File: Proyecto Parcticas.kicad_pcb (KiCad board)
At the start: 2 copper layers, 53.4 x 79.4 mm, 18 parts, among them J2 Molex_KK-254_AE-6410-06A_1x06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, U1 Sensor_de_corriente_ACS758LCB

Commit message: Ultima version
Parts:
- added C4: 100nF, Capacitor_SMD:C_1206_3216Metric, F.Cu at (157.7, 110.2)
- added D1: 1N4752, Diode_SMD:D_MiniMELF, F.Cu at (161.8, 129.0)
- added J3: Baterias, Connector_Molex:Molex_KK-254_AE-6410-02A_1x02_P2.54mm_Vertical, B.Cu at (182.8, 136.4)
- added R1: 100k, Resistor_SMD:R_1206_3216Metric, F.Cu at (157.7, 135.4)
- added R2: 100k, Resistor_SMD:R_1206_3216Metric, F.Cu at (157.7, 132.8)
- added R3: 1M, Resistor_SMD:R_1206_3216Metric, F.Cu at (157.7, 130.3)
- added R4: 100k, Resistor_SMD:R_1206_3216Metric, F.Cu at (157.7, 127.5)
- C2, C3: moved to B.Cu
- moved C3 41.0 mm to (182.5, 100.0), turned to 90 degrees
- moved C2 28.0 mm to (140.5, 78.6), turned to 90 degrees
- moved S1 1.70 mm to (182.9, 125.5)
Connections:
- C2 pad 1: VCC -> unconnected-(C2-Pad1)
- C3 pad 1: EN -> Net-(C3-Pad1)
- E1 pad 1: E_CLK -> (no net)
- E1 pad 2: E_DT -> (no net)
- E1 pad 3: E_SW -> (no net)
- E1 pad 4: VCC -> (no net)
- E1 pad 5: GND -> (no net)
- S2 pad : B+ -> (no net)
- S2 pad 1: A+ -> Net-(S2-Pad1)
- S2 pad 2: A- -> Net-(S2-Pad2)
- S2 pad 3: E+ -> Net-(S2-Pad3)
- S2 pad 4: E- -> Net-(S2-Pad4)
- S3 pad 1: E+ -> (no net)
- S3 pad 2: E- -> (no net)
- S3 pad 3: A- -> (no net)
- S3 pad 4: A+ -> (no net)
- U1 pad 1: GND -> (no net)
- U1 pad 2: VCC -> (no net)
- U1 pad 3: S_C_OU1 -> (no net)
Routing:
- net GND: track 234.2 -> 316.7 mm, vias 0 -> 2
- net Net-(C3-Pad1): track 0.00 -> 69.9 mm
- net BAText+: track 0.00 -> 33.3 mm
- net BATint+: track 0.00 -> 27.9 mm
- net EN: track 9.46 -> 34.7 mm
- net Net-(S2-Pad3): track 0.00 -> 10.7 mm
- net E+: track 10.7 -> 0.00 mm
- net Net-(S2-Pad4): track 0.00 -> 10.7 mm
- net E-: track 10.7 -> 0.00 mm
- net Net-(S2-Pad2): track 0.00 -> 10.7 mm
- net A-: track 10.7 -> 0.00 mm
- net Net-(S2-Pad1): track 0.00 -> 10.7 mm
- net A+: track 10.7 -> 0.00 mm
- net BAT+_EXT: track 0.00 -> 8.80 mm
- net BAT+_INT: track 0.00 -> 8.55 mm
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
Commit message: Ultima super mejorada
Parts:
- removed the REF** at (145.0, 115.3)
- removed the REF** at (177.7, 119.3)
- removed the REF** at (146.2, 120.1)
- removed uC1: Esp32s, Esp32:Esp32
- added ?: , , F.Cu at (183.9, 139.2)
- added ?: , , F.Cu at (142.7, 69.8)
- added ?: , , F.Cu at (183.9, 69.8)
- added ?: , , F.Cu at (143.0, 139.2)
- moved C2 45.4 mm to (180.1, 100.8), turned to 180 degrees
- moved S1 19.5 mm to (180.1, 106.2)
- moved J2 7.15 mm to (180.1, 115.3)
- moved C3 5.75 mm to (180.1, 94.7), turned to 180 degrees
- moved J3 5.11 mm to (180.1, 132.1), turned to -90 degrees
- moved U1 4.75 mm to (144.0, 128.2)
- moved Entrada_Alim. 4.58 mm to (143.9, 134.6)
- moved DS1 4.55 mm to (144.0, 119.1)
- moved E1 4.00 mm to (144.0, 102.4)
- moved S2 1.67 mm to (159.7, 78.5)
- moved S3 0.41 mm to (183.1, 74.9)
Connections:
- C2 pad 1: unconnected-(C2-Pad1) -> VCC
- C3 pad 1: Net-(C3-Pad1) -> EN
- D1 pad 1: BAText+ -> GND
- E1 pad 1: (no net) -> E_CLK
- E1 pad 2: (no net) -> E_DT
- E1 pad 3: (no net) -> E_SW
- E1 pad 4: (no net) -> VCC
- E1 pad 5: (no net) -> GND
- J3 pad 2: BAText+ -> BATint+
- R3 pad 1: BAText+ -> GND
- S3 pad 1: (no net) -> Net-(S2-Pad3)
- S3 pad 2: (no net) -> Net-(S2-Pad4)
- S3 pad 3: (no net) -> Net-(S2-Pad2)
- S3 pad 4: (no net) -> Net-(S2-Pad1)
- U1 pad 1: (no net) -> GND
- U1 pad 2: (no net) -> VCC
- U1 pad 3: (no net) -> S_C_OU1
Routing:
- net Net-(C3-Pad1): track 69.9 -> 0.00 mm
- net EN: track 34.7 -> 82.9 mm, vias 0 -> 1
- net BAText+: track 33.3 -> 0.00 mm
- net S_I_OUT: track 34.1 -> 7.98 mm
- net D_SDA: track 14.3 -> 7.01 mm
- net SD_SCK: track 11.7 -> 6.38 mm
- net SD_CS: track 11.7 -> 6.38 mm
- net VCC: track 163.5 -> 158.5 mm, vias 0 -> 2
- net D_DC: track 18.9 -> 14.1 mm
- net D_RES: track 11.0 -> 14.8 mm, vias 0 -> 2
- net E_SW: track 12.0 -> 8.51 mm
- net D_SCL: track 10.7 -> 7.22 mm
- net SD_MISO: track 10.7 -> 7.44 mm
- net GND: track 316.7 -> 313.5 mm, vias 2 -> 6
- net S_C_OU1: track 10.8 -> 8.19 mm
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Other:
- board size 53.4 x 79.4 mm -> 46.7 x 74.5 mm

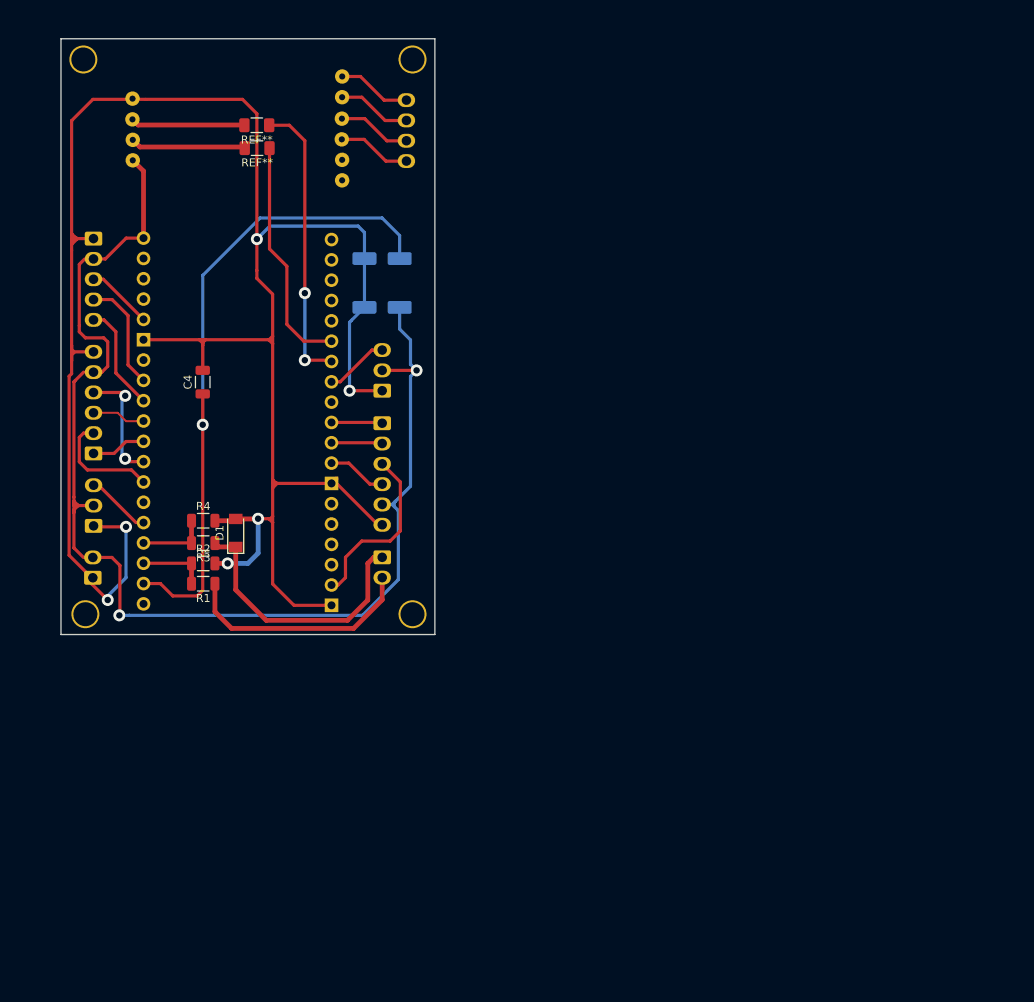
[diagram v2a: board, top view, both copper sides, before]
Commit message: <Arreglo divisor de tensión baterias>
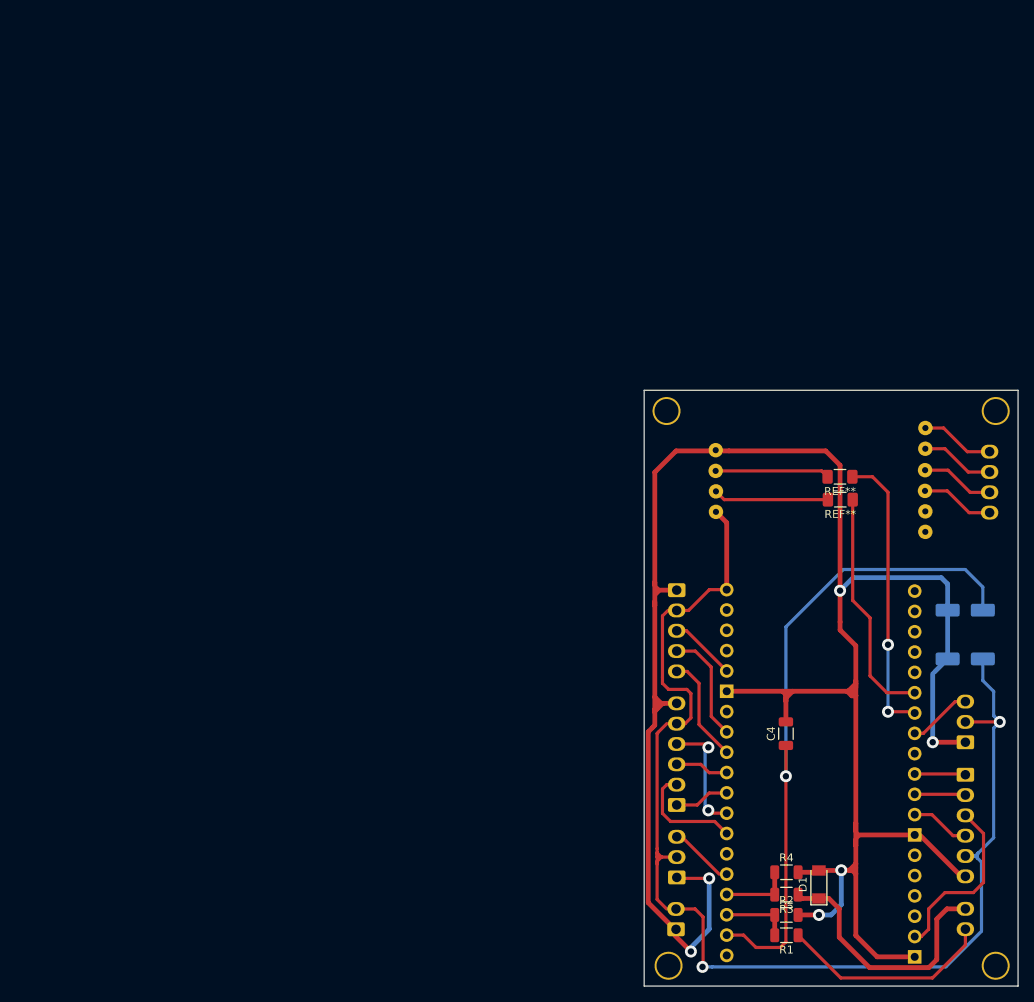
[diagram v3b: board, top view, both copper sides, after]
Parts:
- removed the ? at (183.9, 139.2)
- removed the ? at (142.7, 69.8)
- removed the ? at (183.9, 69.8)
- removed the ? at (143.0, 139.2)
- removed the REF** at (164.5, 80.9)
- removed the REF** at (164.4, 78.1)
- removed the REF** at (150.3, 92.2)
- removed the REF** at (173.8, 138.1)
- added ?: , , F.Cu at (256.8, 183.1)
- added ?: , , F.Cu at (215.6, 113.8)
- added ?: , , F.Cu at (215.9, 183.1)
- added ?: , , F.Cu at (256.8, 113.8)
- added REF**: R_1206_3216Metric_Pad1.30x1.75mm_HandSolder, Resistor_SMD:R_1206_3216Metric_Pad1.30x1.75mm_HandSolder, F.Cu at (237.4, 124.9)
- added REF**: R_1206_3216Metric_Pad1.30x1.75mm_HandSolder, Resistor_SMD:R_1206_3216Metric_Pad1.30x1.75mm_HandSolder, F.Cu at (237.3, 122.0)
- added REF**: PinHeader_1x19_P2.54mm_Vertical, Connector_PinHeader_2.54mm:PinHeader_1x19_P2.54mm_Vertical, B.Cu at (223.2, 136.1)
- added REF**: PinHeader_1x19_P2.54mm_Vertical, Connector_PinHeader_2.54mm:PinHeader_1x19_P2.54mm_Vertical, B.Cu at (246.7, 182.0)
- moved C4 85.1 mm to (230.6, 154.1)
- moved C2 85.1 mm to (253.0, 144.8)
- moved C3 85.1 mm to (253.0, 138.7)
- moved DS1 85.1 mm to (216.9, 163.0)
- moved E1 85.1 mm to (216.9, 146.3)
- moved Entrada_Alim. 85.1 mm to (216.8, 178.6)
- moved J2 85.1 mm to (253.0, 159.3)
- moved R1 85.1 mm to (230.6, 179.3)
- moved R3 85.1 mm to (230.6, 174.2)
- moved R4 85.1 mm to (230.6, 171.4)
- moved S1 85.1 mm to (253.0, 150.1)
- moved S2 85.1 mm to (232.6, 122.5)
- moved S3 85.1 mm to (256.0, 118.9)
- moved U1 85.1 mm to (216.9, 172.1)
- moved D1 85.1 mm to (234.7, 173.0)
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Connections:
- D1 pad 1: GND -> BAText+
- J3 pad : GND -> BAText+
- R3 pad 1: GND -> BAText+
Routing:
- net BAText+: track 0.00 -> 33.8 mm
- net GND: track 313.5 -> 295.6 mm
- net BATint+: track 29.5 -> 26.8 mm

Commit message: <Agregué el PWM>
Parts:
- added J3: Baterias, Connector_Molex:Molex_KK-254_AE-6410-02A_1x02_P2.54mm_Vertical, B.Cu at (256.1, 130.6)
- moved C2 0.92 mm to (253.7, 144.3)
- moved C3 0.92 mm to (253.7, 138.2)
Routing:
- net PWM_OUT: track 0.00 -> 54.6 mm, vias 0 -> 1
- net GND: track 295.6 -> 326.8 mm
- net VCC: track 158.5 -> 144.9 mm, vias 2 -> 0
- net EN: track 82.9 -> 80.3 mm

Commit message: <Revisión PCB y STEP>
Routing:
- net VCC: track 144.9 -> 150.2 mm, vias 0 -> 2
- net SD_MOSI: track 22.2 -> 26.4 mm
- net GND: track 326.8 -> 329.3 mm
- net PWM_OUT: track 54.6 -> 55.6 mm
- net BAText+: track 33.8 -> 34.4 mm
